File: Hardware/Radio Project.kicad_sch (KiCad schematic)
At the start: 33 parts, among them SW1 208-4, U1 STM32F407VGT6

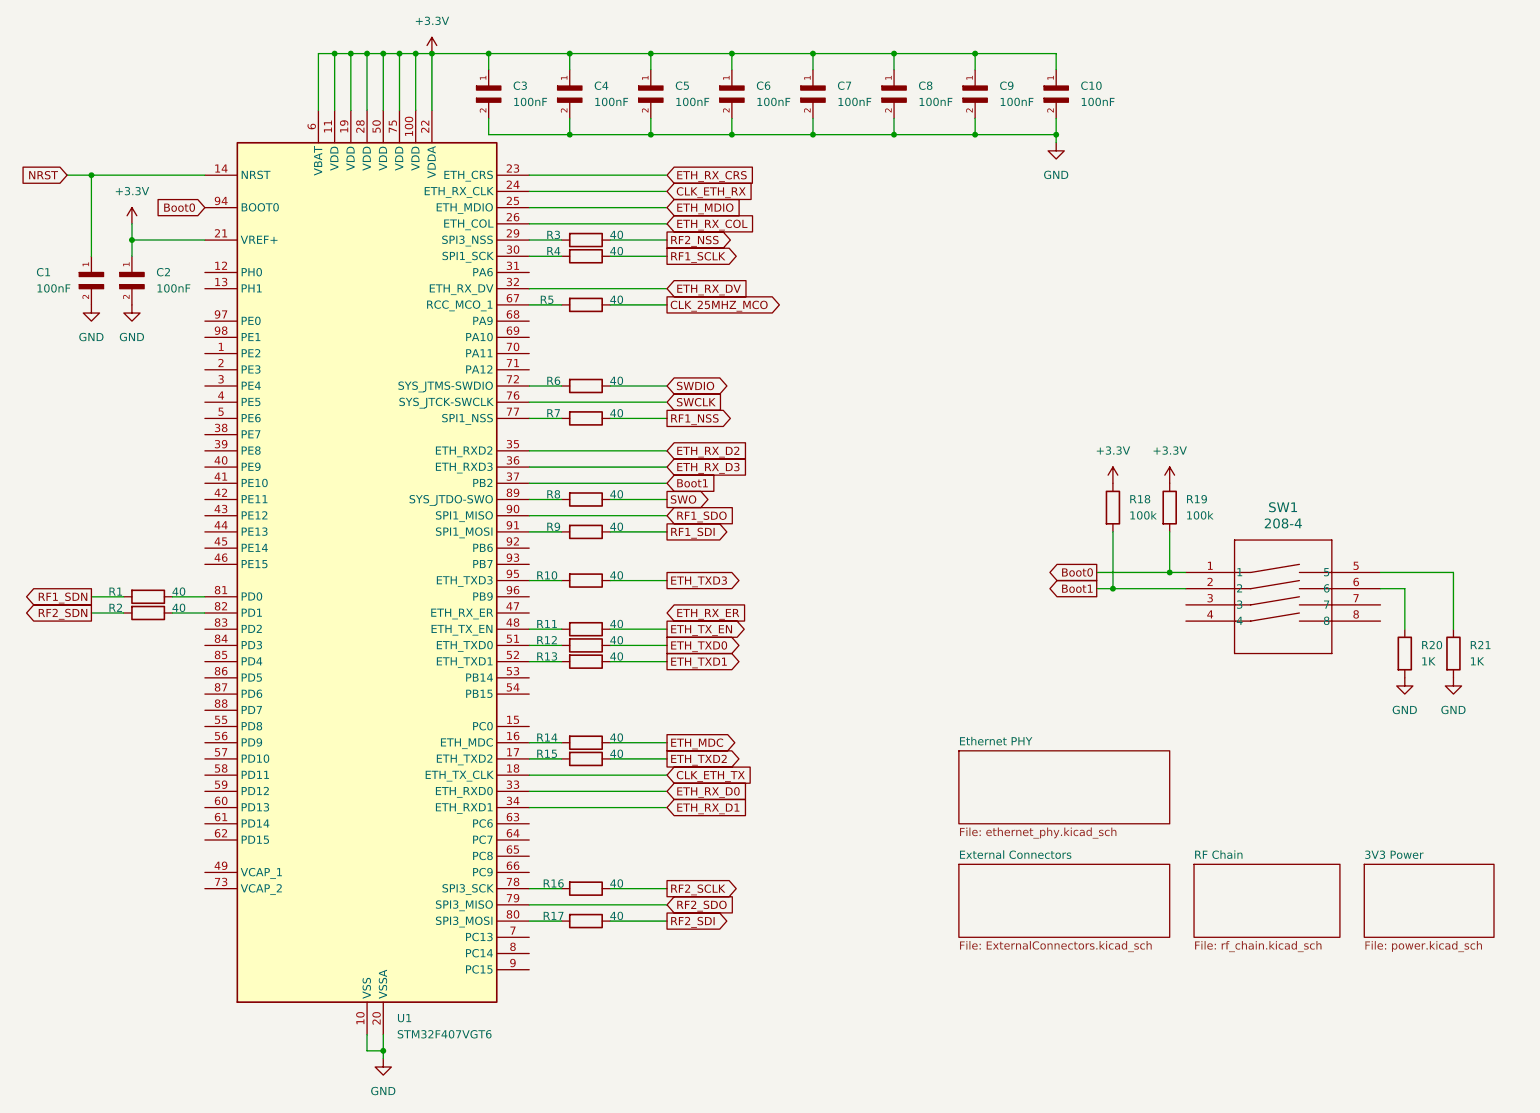
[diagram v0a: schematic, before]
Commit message: Added oscillators, reset button, and finalized ETH connection
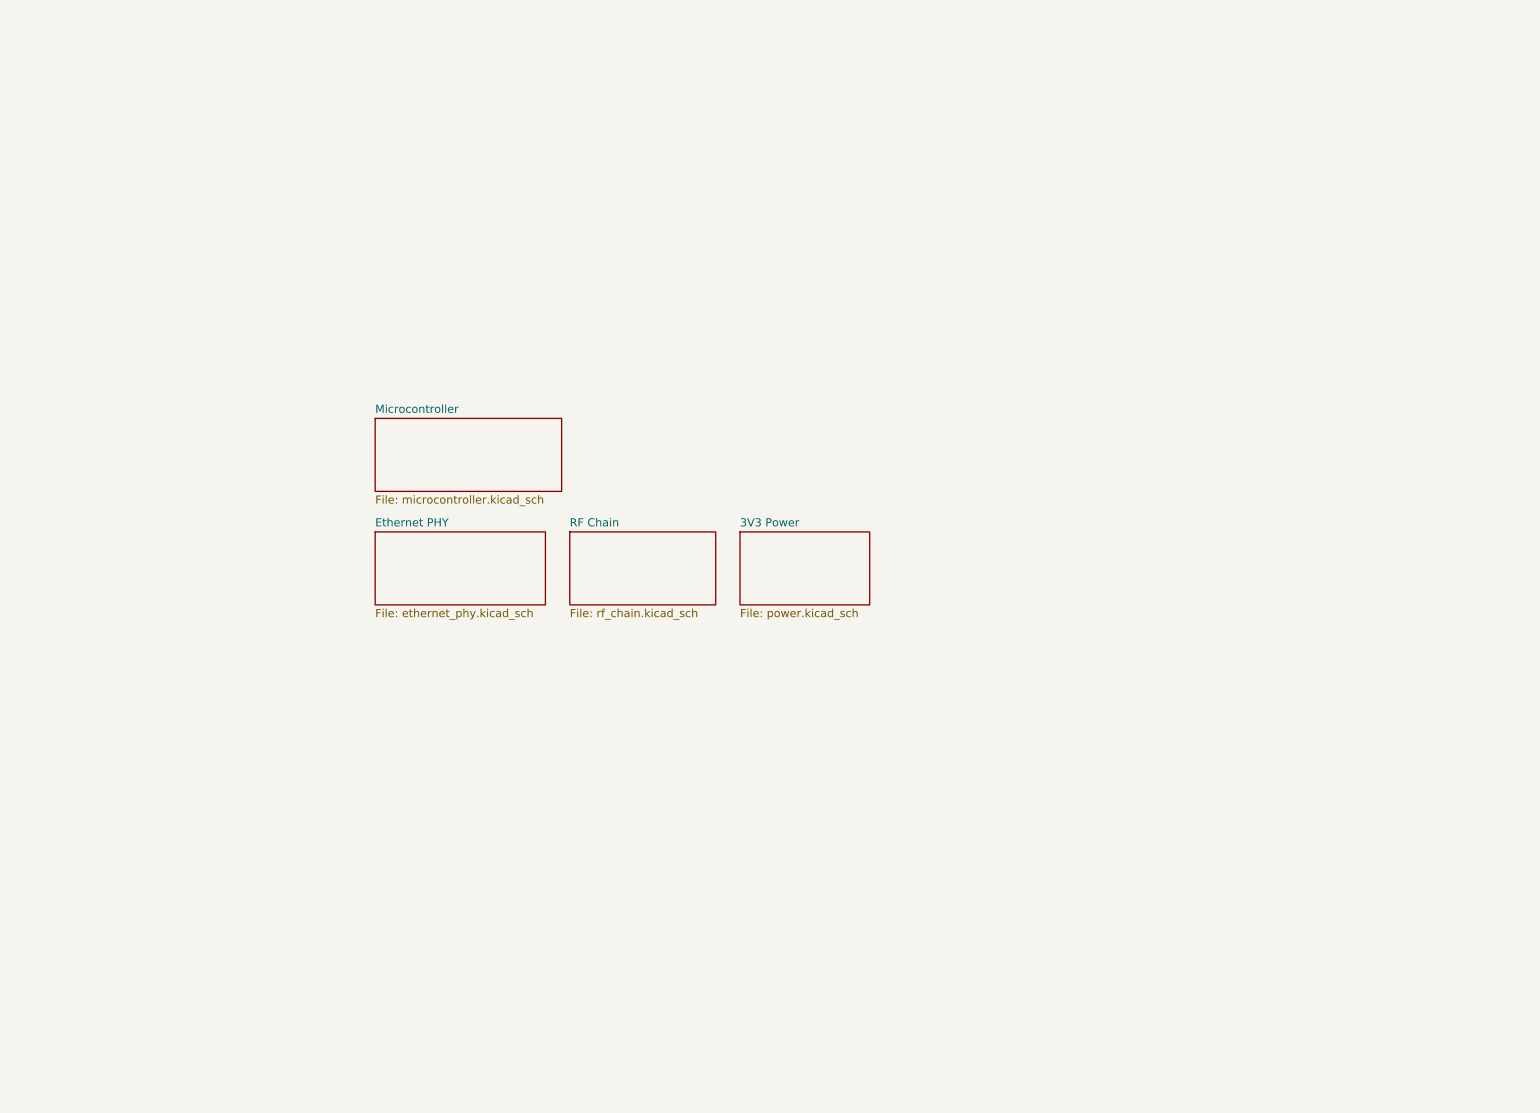
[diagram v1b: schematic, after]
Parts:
- removed C1, C10, C2, C3, C4, C5, C6, C7, C8, C9: 100nF, C0402C104J8RACTU:CAPC10555_55N_KEM-L, symbol 2025-06-22_21-59-05:C0402C104J8RACTU
- removed R1, R10, R11, R12, R13, R14, R15, R16, R17, R2, R3, R4, R5, R6, R7, R8, R9: 40, Resistor_SMD:R_0402_1005Metric, symbol Device:R
- removed R18, R19: 100k, Resistor_SMD:R_0402_1005Metric, symbol Device:R
- removed R20, R21: 1K, Resistor_SMD:R_0402_1005Metric, symbol Device:R
- removed SW1: 208-4, 208-4:DIP8_208-4_CTS, symbol 4 POS Dip Switch:208-4
- removed U1: STM32F407VGT6, Package_QFP:LQFP-100_14x14mm_P0.5mm, symbol MCU_ST_STM32F4:STM32F407VGTx
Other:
- removed sheet External Connectors
- added sheet Microcontroller (microcontroller.kicad_sch)
